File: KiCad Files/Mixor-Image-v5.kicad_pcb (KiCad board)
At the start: 2 copper layers, 60.6 x 46 mm, 80 parts, among them J1 Conn_01x03_Male, J2 Conn_01x03_Female, J3 Conn_01x03_Male, J4 Conn_01x03_Female, U1 TL072, U2 TL072

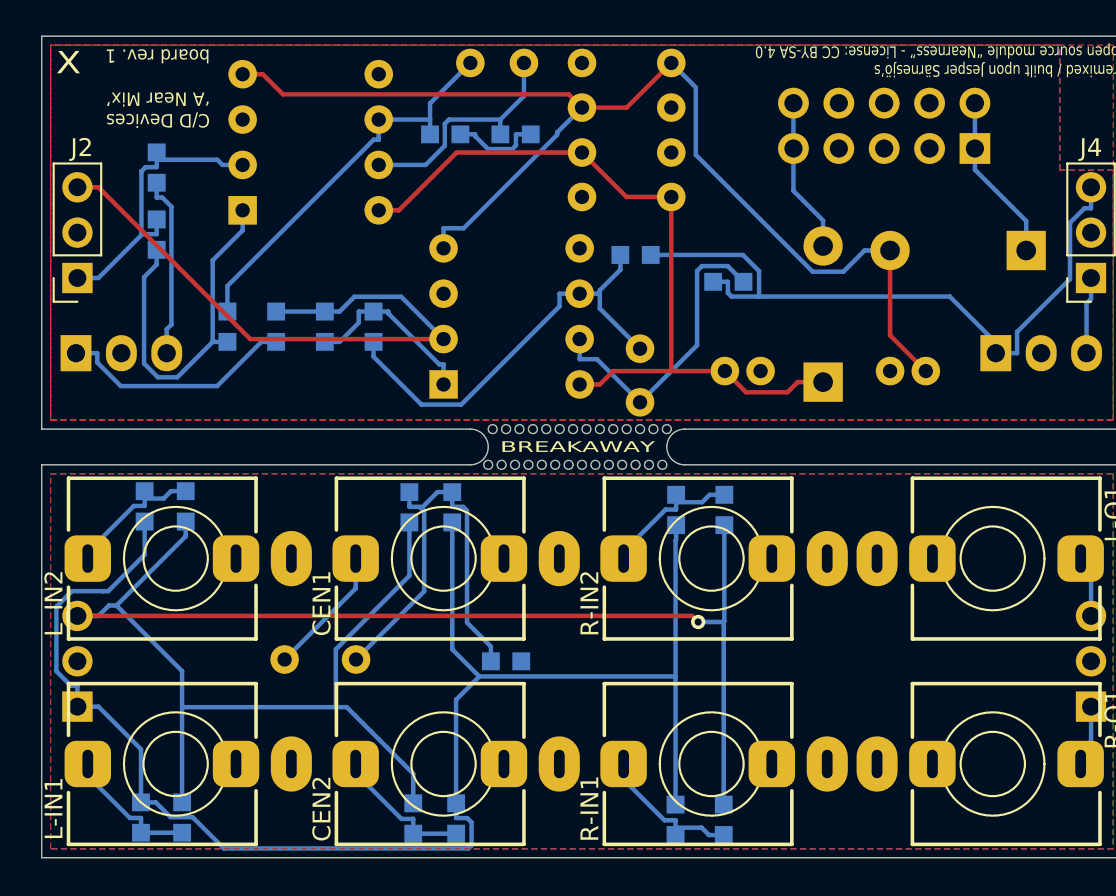
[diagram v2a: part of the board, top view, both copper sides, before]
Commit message: updated panel with C/D graphics
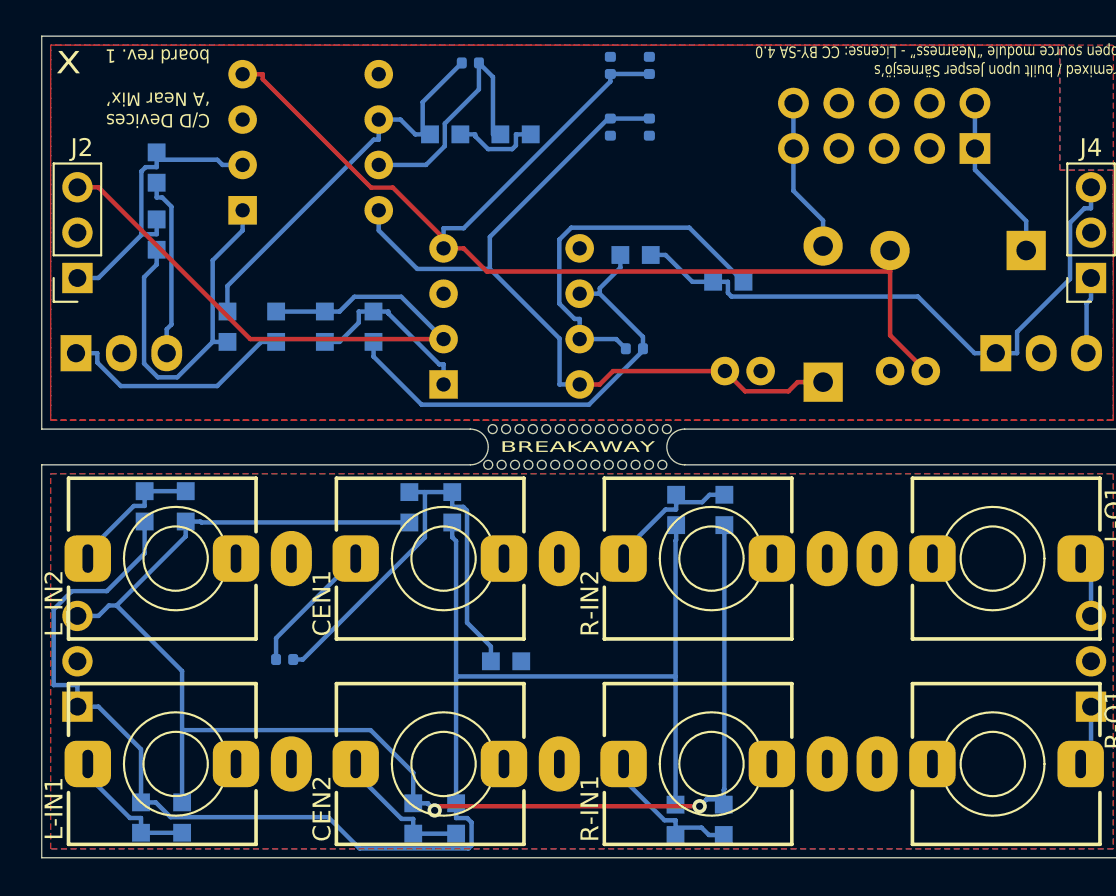
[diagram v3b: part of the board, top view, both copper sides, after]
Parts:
- C1: footprint Capacitor_THT:C_Rect_L4.0mm_W2.0mm_P4.00mm -> Capacitor_SMD:C_0402_1005Metric
- C2, C3: footprint Capacitor_THT:C_Disc_D4.0mm_W1.6mm_P3.0mm -> Capacitor_SMD:C_0402_1005Metric
- C6, C7, C8, C9: footprint Capacitor_THT:C_Disc_D4.3mm_W1.9mm_P5.00mm -> Capacitor_SMD:C_0402_1005Metric
- moved C6 4.10 mm to (151.5, 83.3), turned to -90 degrees
- moved C7 2.66 mm to (151.5, 79.9), turned to -90 degrees
- moved C8 2.13 mm to (149.3, 83.3), turned to -90 degrees
- moved C9 1.59 mm to (149.3, 79.9), turned to -90 degrees
- moved C3 0.32 mm to (150.6, 95.7), turned to 180 degrees
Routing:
- net Net-(J1-Pin_3): track 101.5 -> 83.0 mm, vias 1 -> 2
- net Net-(J4-Pin_3): track 38.7 -> 34.4 mm
- net Net-(C3-Pad2): track 17.3 -> 20.9 mm
- net +12V: track 43.2 -> 45.5 mm
- net Net-(U2B--): track 24.3 -> 26.2 mm
- net Net-(C1-Pad2): track 24.5 -> 25.9 mm
- net Net-(C2-Pad2): track 13.1 -> 14.3 mm
- net Net-(J1-Pin_1): track 88.1 -> 89.0 mm
- net -12V: track 64.9 -> 65.6 mm
